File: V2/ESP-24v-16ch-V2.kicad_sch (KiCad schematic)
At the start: 8 parts, among them J1 Conn_01x08, J2 Conn_01x08, J3 Conn_01x08, J4 Conn_01x08, J5 Conn_01x08, J6 Conn_01x08, J7 Conn_01x08, J8 Conn_01x08

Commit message: Updated references
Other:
- sheet GPIO Expanders: file ESP-24v-16ch-V1-expanders.kicad_sch -> ESP-24v-16ch-V2-expanders.kicad_sch
- sheet Inputs 1-16: file ESP-24v-16ch-V1-inputs-1.kicad_sch -> ESP-24v-16ch-V2-inputs-1.kicad_sch
- sheet Inputs 17-32: file ESP-24v-16ch-V1-inputs-2.kicad_sch -> ESP-24v-16ch-V2-inputs-2.kicad_sch
- sheet LAN: file ESP-24v-16ch-V1-lan.kicad_sch -> ESP-24v-16ch-V2-lan.kicad_sch
- sheet MCU: file ESP-24v-16ch-V1-mcu.kicad_sch -> ESP-24v-16ch-V2-mcu.kicad_sch
- sheet Outputs 1-16: file ESP-24v-16ch-V1-outputs-1.kicad_sch -> ESP-24v-16ch-V2-outputs-1.kicad_sch
- sheet Outputs 17-32: file ESP-24v-16ch-V1-outputs-2.kicad_sch -> ESP-24v-16ch-V2-outputs-2.kicad_sch
- sheet Power: file ESP-24v-16ch-V1-power.kicad_sch -> ESP-24v-16ch-V2-power.kicad_sch
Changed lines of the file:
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@@
     (pin "8")
     (instances
-      (project "ESP-24v-16ch-V1"
+      (project "ESP-24v-16ch-V2"
         (path "/2bc5a21a-1d79-419d-a592-6852cc07b00a"
           (reference "J6") (unit 1)
@@
     (pin "8")
     (instances
-      (project "ESP-24v-16ch-V1"
+      (project "ESP-24v-16ch-V2"
         (path "/2bc5a21a-1d79-419d-a592-6852cc07b00a"
           (reference "J7") (unit 1)
@@
     (pin "8")
     (instances
-      (project "ESP-24v-16ch-V1"
+      (project "ESP-24v-16ch-V2"
         (path "/2bc5a21a-1d79-419d-a592-6852cc07b00a"
           (reference "J5") (unit 1)
@@
     (pin "8")
     (instances
-      (project "ESP-24v-16ch-V1"
+      (project "ESP-24v-16ch-V2"
         (path "/2bc5a21a-1d79-419d-a592-6852cc07b00a"
           (reference "J2") (unit 1)
@@
     (pin "8")
     (instances
-      (project "ESP-24v-16ch-V1"
+      (project "ESP-24v-16ch-V2"
         (path "/2bc5a21a-1d79-419d-a592-6852cc07b00a"
           (reference "J1") (unit 1)
@@
     (pin "8")
     (instances
-      (project "ESP-24v-16ch-V1"
+      (project "ESP-24v-16ch-V2"
         (path "/2bc5a21a-1d79-419d-a592-6852cc07b00a"
           (reference "J8") (unit 1)
@@
     (pin "8")
     (instances
-      (project "ESP-24v-16ch-V1"
+      (project "ESP-24v-16ch-V2"
         (path "/2bc5a21a-1d79-419d-a592-6852cc07b00a"
           (reference "J3") (unit 1)
@@
     (pin "8")
     (instances
-      (project "ESP-24v-16ch-V1"
+      (project "ESP-24v-16ch-V2"
         (path "/2bc5a21a-1d79-419d-a592-6852cc07b00a"
           (reference "J4") (unit 1)
@@
       (effects (font (size 1.27 1.27)) (justify left bottom))
     )
-    (property "Sheetfile" "ESP-24v-16ch-V1-inputs-2.kicad_sch" (at 60.96 155.5246 0)
+    (property "Sheetfile" "ESP-24v-16ch-V2-inputs-2.kicad_sch" (at 60.96 155.5246 0)
       (effects (font (size 1.27 1.27)) (justify left top))
     )
@@
     )
     (instances
-      (project "ESP-24v-16ch-V1"
+      (project "ESP-24v-16ch-V2"
         (path "/2bc5a21a-1d79-419d-a592-6852cc07b00a" (page "7"))
       )
@@
       (effects (font (size 1.27 1.27)) (justify left bottom))
     )
-    (property "Sheetfile" "ESP-24v-16ch-V1-outputs-1.kicad_sch" (at 198.12 104.7246 0)
+    (property "Sheetfile" "ESP-24v-16ch-V2-outputs-1.kicad_sch" (at 198.12 104.7246 0)
       (effects (font (size 1.27 1.27)) (justify left top))
     )
@@
     )
     (instances
-      (project "ESP-24v-16ch-V1"
+      (project "ESP-24v-16ch-V2"
         (path "/2bc5a21a-1d79-419d-a592-6852cc07b00a" (page "8"))
       )
@@
       (effects (font (size 1.27 1.27)) (justify left bottom))
     )
-    (property "Sheetfile" "ESP-24v-16ch-V1-power.kicad_sch" (at 60.96 36.1446 0)
+    (property "Sheetfile" "ESP-24v-16ch-V2-power.kicad_sch" (at 60.96 36.1446 0)
       (effects (font (size 1.27 1.27)) (justify left top))
     )
@@
     )
     (instances
-      (project "ESP-24v-16ch-V1"
+      (project "ESP-24v-16ch-V2"
         (path "/2bc5a21a-1d79-419d-a592-6852cc07b00a" (page "2"))
       )
@@
       (effects (font (size 1.27 1.27)) (justify left bottom))
     )
-    (property "Sheetfile" "ESP-24v-16ch-V1-inputs-1.kicad_sch" (at 60.96 104.7246 0)
+    (property "Sheetfile" "ESP-24v-16ch-V2-inputs-1.kicad_sch" (at 60.96 104.7246 0)
       (effects (font (size 1.27 1.27)) (justify left top))
     )
@@
     )
     (instances
-      (project "ESP-24v-16ch-V1"
+      (project "ESP-24v-16ch-V2"
         (path "/2bc5a21a-1d79-419d-a592-6852cc07b00a" (page "6"))
       )
@@
       (effects (font (size 1.27 1.27)) (justify left bottom))
     )
-    (property "Sheetfile" "ESP-24v-16ch-V1-expanders.kicad_sch" (at 109.22 155.5246 0)
+    (property "Sheetfile" "ESP-24v-16ch-V2-expanders.kicad_sch" (at 109.22 155.5246 0)
       (effects (font (size 1.27 1.27)) (justify left top))
     )
@@
     )
     (instances
-      (project "ESP-24v-16ch-V1"
+      (project "ESP-24v-16ch-V2"
         (path "/2bc5a21a-1d79-419d-a592-6852cc07b00a" (page "5"))
       )
@@
       (effects (font (size 1.27 1.27)) (justify left bottom))
     )
-    (property "Sheetfile" "ESP-24v-16ch-V1-lan.kicad_sch" (at 198.12 51.3846 0)
+    (property "Sheetfile" "ESP-24v-16ch-V2-lan.kicad_sch" (at 198.12 51.3846 0)
       (effects (font (size 1.27 1.27)) (justify left top))
     )
@@
     )
     (instances
-      (project "ESP-24v-16ch-V1"
+      (project "ESP-24v-16ch-V2"
         (path "/2bc5a21a-1d79-419d-a592-6852cc07b00a" (page "4"))
       )
@@
       (effects (font (size 1.27 1.27)) (justify left bottom))
     )
-    (property "Sheetfile" "ESP-24v-16ch-V1-outputs-2.kicad_sch" (at 198.12 155.5246 0)
+    (property "Sheetfile" "ESP-24v-16ch-V2-outputs-2.kicad_sch" (at 198.12 155.5246 0)
       (effects (font (size 1.27 1.27)) (justify left top))
     )
@@
     )
     (instances
-      (project "ESP-24v-16ch-V1"
+      (project "ESP-24v-16ch-V2"
         (path "/2bc5a21a-1d79-419d-a592-6852cc07b00a" (page "9"))
       )
@@
       (effects (font (size 1.27 1.27)) (justify left bottom))
     )
-    (property "Sheetfile" "ESP-24v-16ch-V1-mcu.kicad_sch" (at 109.22 51.3846 0)
+    (property "Sheetfile" "ESP-24v-16ch-V2-mcu.kicad_sch" (at 109.22 51.3846 0)
       (effects (font (size 1.27 1.27)) (justify left top))
     )
@@
     )
     (instances
-      (project "ESP-24v-16ch-V1"
+      (project "ESP-24v-16ch-V2"
         (path "/2bc5a21a-1d79-419d-a592-6852cc07b00a" (page "3"))
       )

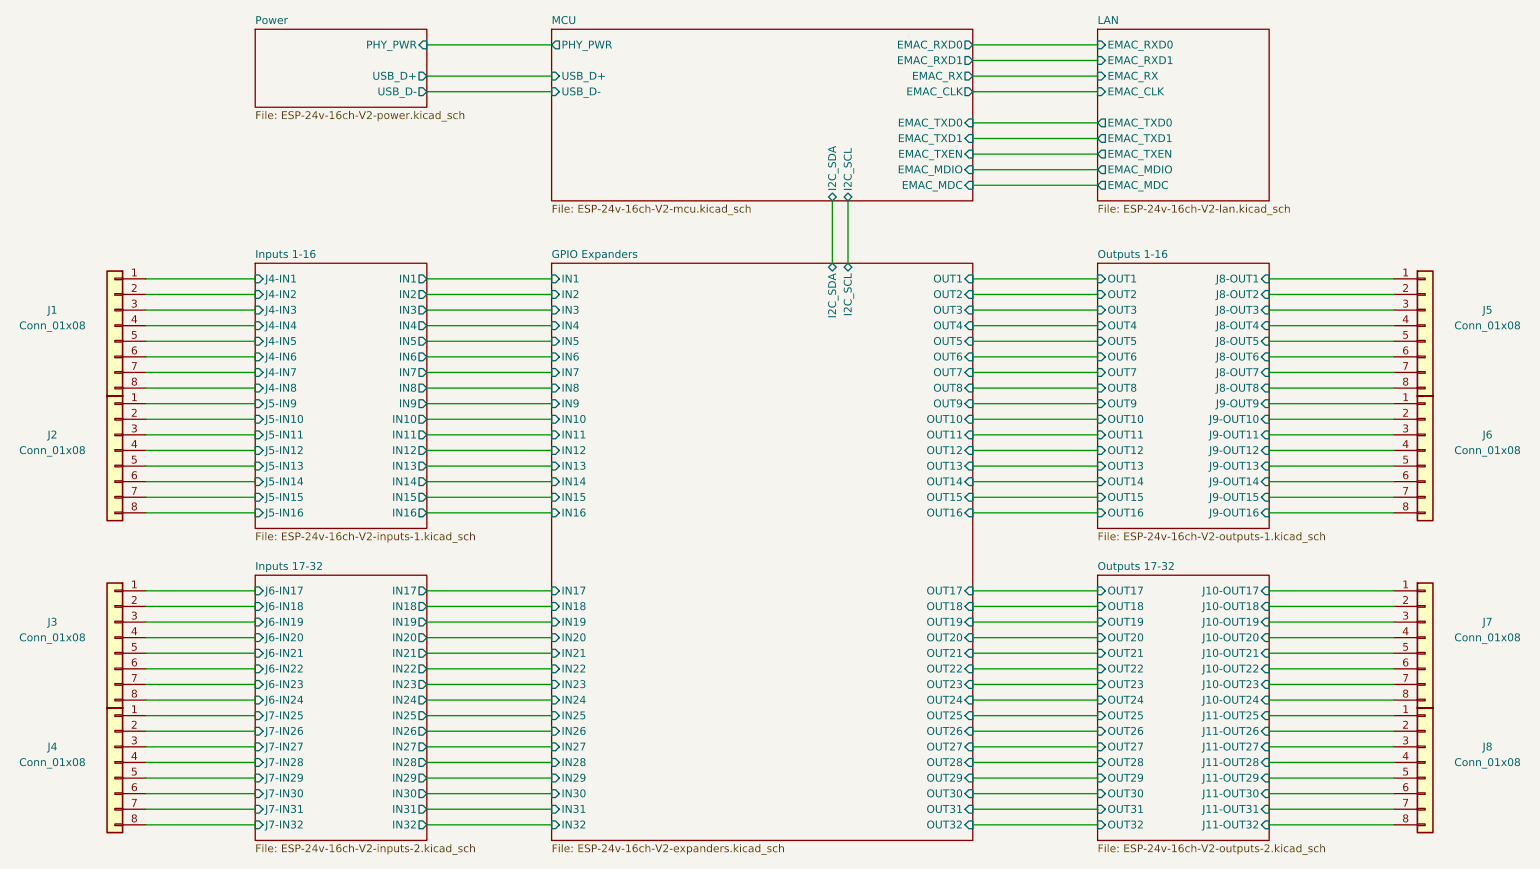
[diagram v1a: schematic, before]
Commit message: Add interrupt pins
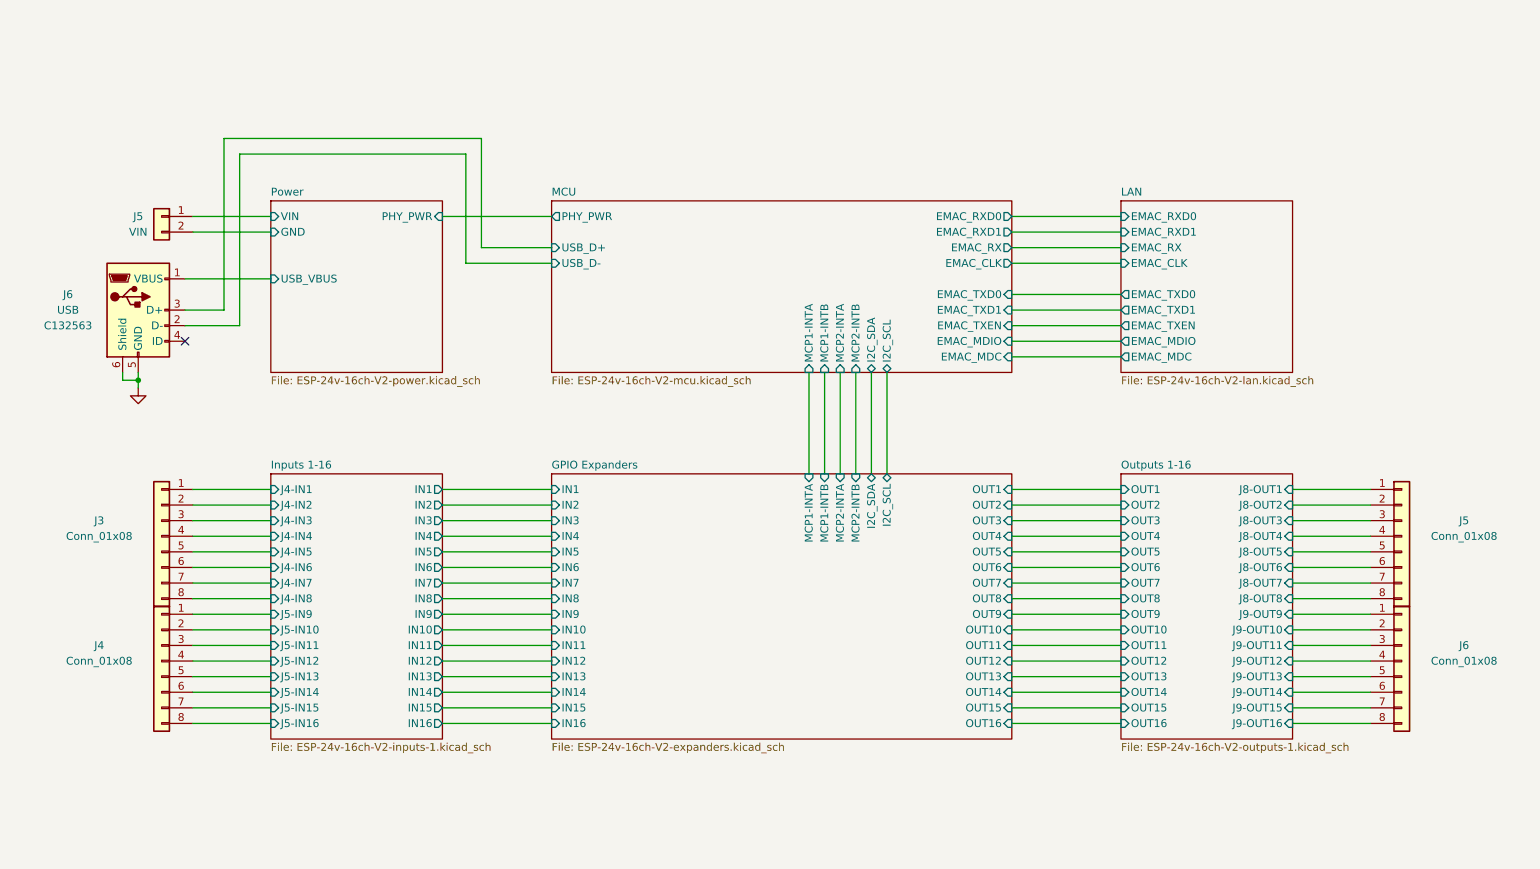
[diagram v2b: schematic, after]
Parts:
- removed J3, J4, J7, J8: Conn_01x08, Tales:TerminalBlock_Dorabo_DB141V-2.54-08P_1x08_P2.54mm_Vertical, symbol Connector_Generic:Conn_01x08
- added J5: VIN, Tales:TerminalBlock_Phoenix_MKDS-3-2-5.08_1x02_P5.08mm_Horizontal, symbol Connector_Generic:Conn_01x02
- added J6: USB, Tales:USB_Micro-B_Amphenol_10104110_Horizontal, symbol Connector:USB_B_Micro
- renumbered J1 to J3, J2 to J4
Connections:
- net MCU/USB_D+: now also J6.3 (D+)
- net MCU/USB_D-: now also J6.2 (D-)
- new net GND: J6.5 (GND), J6.6 (Shield)
- new net Power/GND: J5.2 (Pin_2)
- new net Power/USB_VBUS: J6.1 (VBUS)
- new net Power/VIN: J5.1 (Pin_1)
- no-connect marks 0 -> 1
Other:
- removed sheet Inputs 17-32
- removed sheet Outputs 17-32
- sheet GPIO Expanders ports: added MCP1-INTA, MCP1-INTB, MCP2-INTA, MCP2-INTB; removed IN17, IN18, IN19, IN20, IN21, IN22, IN23, IN24, IN25, IN26, IN27, IN28, IN29, IN30, IN31, IN32, OUT17, OUT18, OUT19, OUT20, OUT21, OUT22, OUT23, OUT24, OUT25, OUT26, OUT27, OUT28, OUT29, OUT30, OUT31, OUT32
- sheet MCU ports: added MCP1-INTA, MCP1-INTB, MCP2-INTA, MCP2-INTB; removed none
- sheet Power ports: added GND, USB_VBUS, VIN; removed USB_D+, USB_D-
- moved on the sheet: J3, J4, J5, J6

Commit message: MCP interrupt signals routed
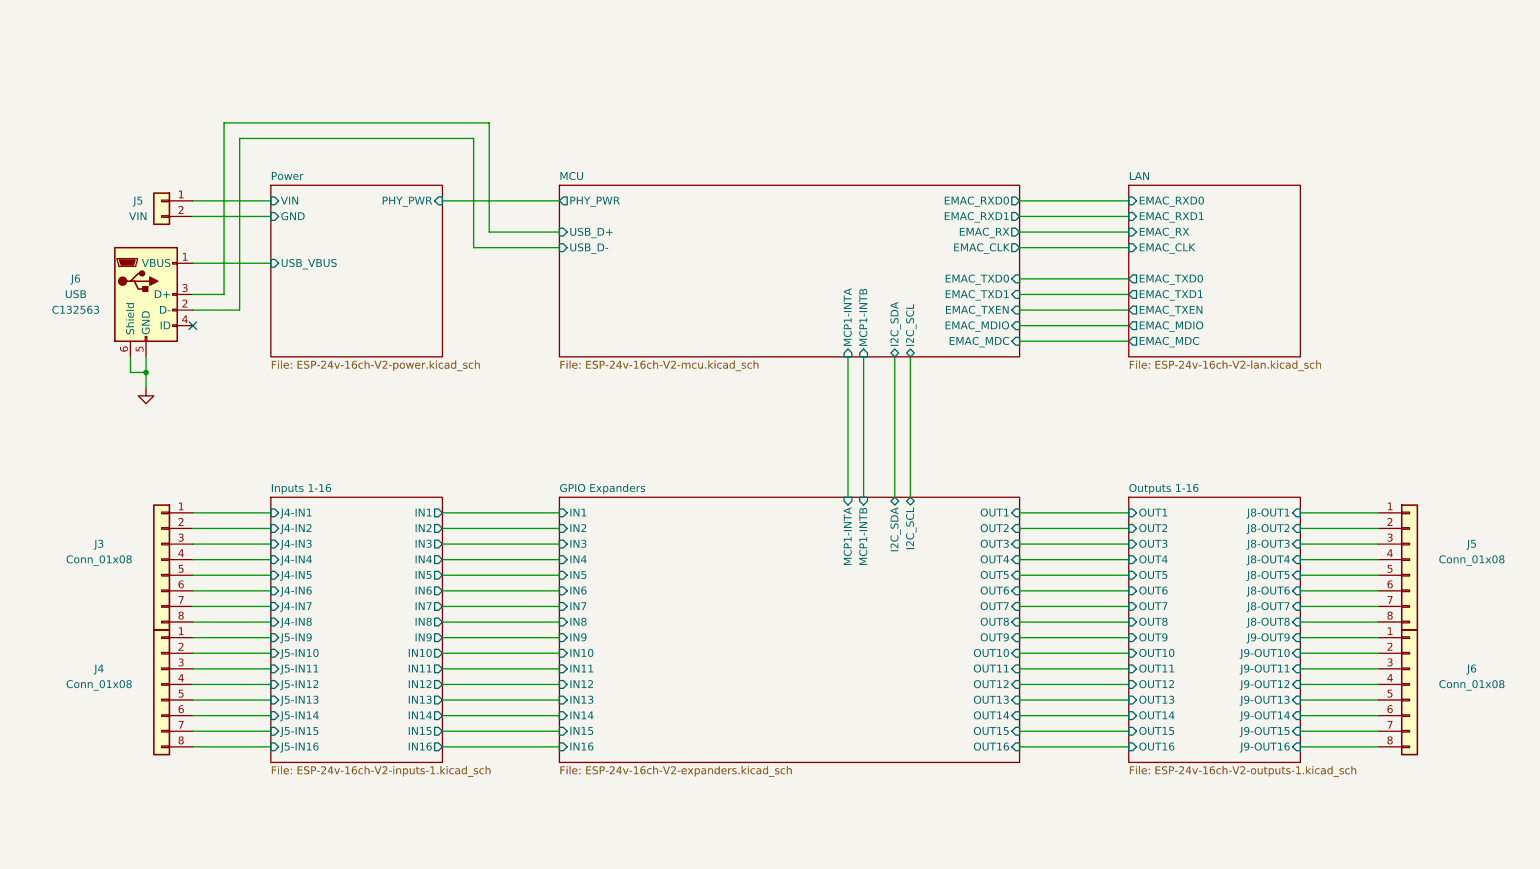
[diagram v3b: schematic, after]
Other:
- sheet GPIO Expanders ports: added none; removed MCP2-INTA, MCP2-INTB
- sheet MCU ports: added none; removed MCP2-INTA, MCP2-INTB
- moved on the sheet: J3, J4, J5, J6

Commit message: Replace connector 3D models
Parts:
- J3, J4, J5, J6: footprint Tales:TerminalBlock_Dorabo_DB141V-2.54-08P_1x08_P2.54mm_Vertical -> Tales:TerminalBlock_DG141V-2.54-8P_1x08_P2.54mm_Vertical
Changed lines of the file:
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@@
       (effects (font (size 1.27 1.27)))
     )
-    (property "Footprint" "Tales:TerminalBlock_Dorabo_DB141V-2.54-08P_1x08_P2.54mm_Vertical" (at 248.92 129.54 0)
+    (property "Footprint" "Tales:TerminalBlock_DG141V-2.54-8P_1x08_P2.54mm_Vertical" (at 248.92 129.54 0)
       (effects (font (size 1.27 1.27)) hide)
     )
@@
       (effects (font (size 1.27 1.27)))
     )
-    (property "Footprint" "Tales:TerminalBlock_Dorabo_DB141V-2.54-08P_1x08_P2.54mm_Vertical" (at 248.92 109.22 0)
+    (property "Footprint" "Tales:TerminalBlock_DG141V-2.54-8P_1x08_P2.54mm_Vertical" (at 248.92 109.22 0)
       (effects (font (size 1.27 1.27)) hide)
     )
@@
       (effects (font (size 1.27 1.27)))
     )
-    (property "Footprint" "Tales:TerminalBlock_Dorabo_DB141V-2.54-08P_1x08_P2.54mm_Vertical" (at 45.72 129.54 0)
+    (property "Footprint" "Tales:TerminalBlock_DG141V-2.54-8P_1x08_P2.54mm_Vertical" (at 45.72 129.54 0)
       (effects (font (size 1.27 1.27)) hide)
     )
@@
       (effects (font (size 1.27 1.27)))
     )
-    (property "Footprint" "Tales:TerminalBlock_Dorabo_DB141V-2.54-08P_1x08_P2.54mm_Vertical" (at 45.72 109.22 0)
-      (effects (font (size 1.27 1.27)) hide)
-    )
+    (property "Footprint" "Tales:TerminalBlock_DG141V-2.54-8P_1x08_P2.54mm_Vertical" (at 45.72 109.22 0)
+      (effects (font (size 1.27 1.27)) hide)
+    )
